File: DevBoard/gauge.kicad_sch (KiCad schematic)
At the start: 52 parts, among them J101 Pack (welded 4S) - use instea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, J102 Cell NTC 10k 103AT, J103 EV2400 SMBus, J104 Bench PACK_P, Q101 AGM404AP1, Q102 AGM404AP1, Q103 2N7002, SW101 WAKE, U101 BQ40Z50RSMR-R2

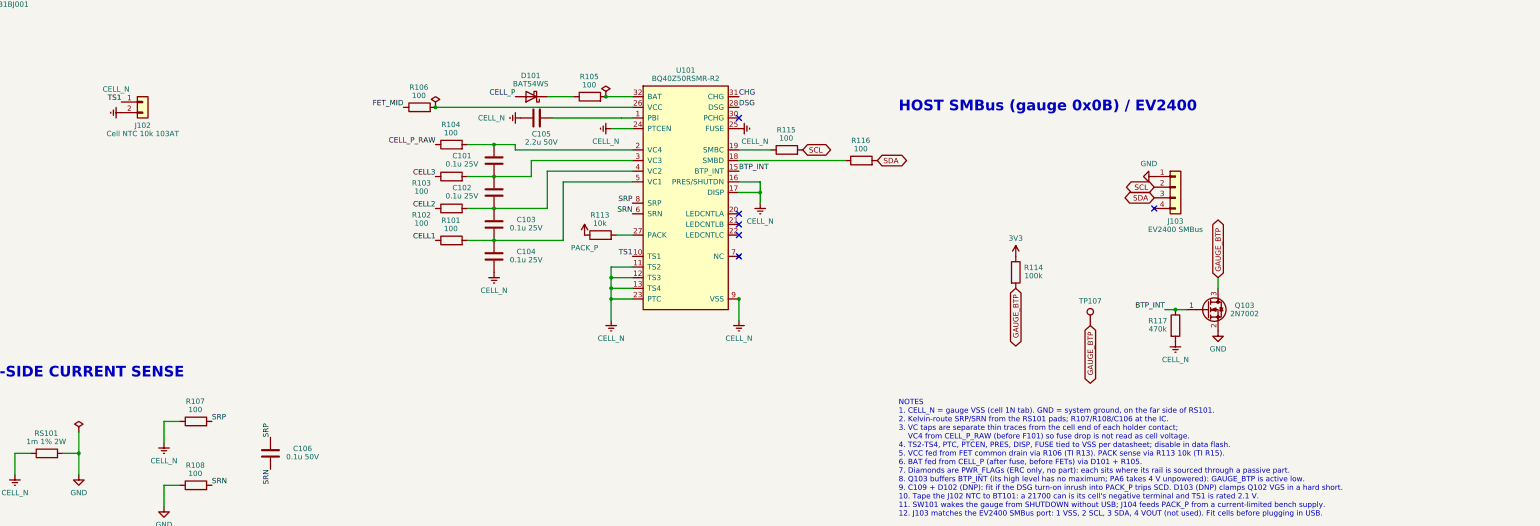
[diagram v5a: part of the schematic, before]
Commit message: Dev board: bootstrap diodes, one NTC per cell, 1 % resistors
- BQ25756 bootstrap Schottkys DRV_SUP -> BTST1/BTST2 on both ports
  (TI BQ25756 schematic checklist D2/D3, required; LRB521S-40T1G,
  SOD-523), placed in line with the BTST caps. Also added to the
  production BOM/netlist.
- Gauge TS2-TS4 no longer tied to VSS: J105-J107 take a wired 10k NTC
  per cell; all four NTC headers sit beside their cell's tap test point.
- Precision resistors rounded to stocked UNI-ROYAL 1 % parts (ICHG
  9.1k, ILIM 3.6k, TS 1.8k/5.6k, FSW/ACUV-ACOV, NTC dividers); only the
  charge-voltage and PP5V feedback dividers stay 0.1 %.

Co-Authored-By: Claude Opus 5.5 <noreply@anthropic.com>
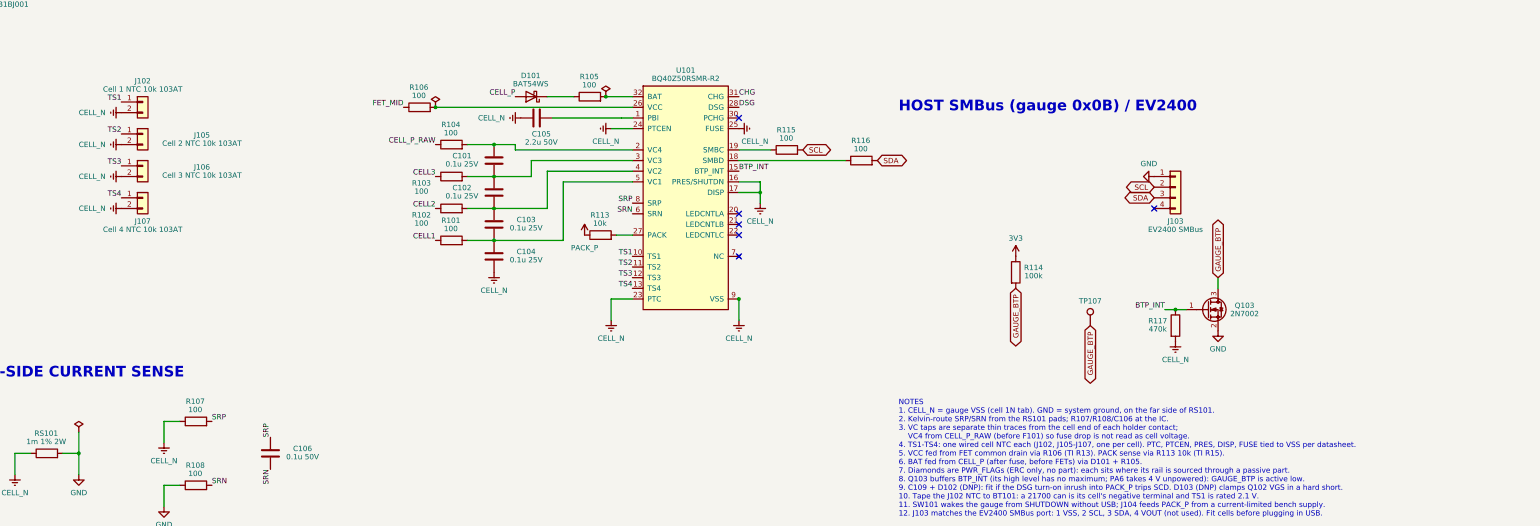
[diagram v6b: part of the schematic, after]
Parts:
- added J105: Cell 2 NTC 10k 103AT, Connector_PinHeader_2.54mm:PinHeader_1x02_P2.54mm_Vertical, symbol Connector_Generic:Conn_01x02
- added J106: Cell 3 NTC 10k 103AT, Connector_PinHeader_2.54mm:PinHeader_1x02_P2.54mm_Vertical, symbol Connector_Generic:Conn_01x02
- added J107: Cell 4 NTC 10k 103AT, Connector_PinHeader_2.54mm:PinHeader_1x02_P2.54mm_Vertical, symbol Connector_Generic:Conn_01x02
- J102: value Cell NTC 10k 103AT -> Cell 1 NTC 10k 103AT; LCSC (none) -> C492401; MPN (none) -> PZ254V-11-02P; Notes (none) -> Wired 10k B3435 NTC (Semitec 103AT-2 class, epoxy bead with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
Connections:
- net CELL_N: now also J105.2 (Pin_2), J106.2 (Pin_2), J107.2 (Pin_2); no longer U101.11 (TS2), U101.12 (TS3), U101.13 (TS4)
- new net TS2: J105.1 (Pin_1), U101.11 (TS2)
- new net TS3: J106.1 (Pin_1), U101.12 (TS3)
- new net TS4: J107.1 (Pin_1), U101.13 (TS4)
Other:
- note added: "NOTES 1. CELL_N = gauge VSS (cell 1N tab). GND = system ground, on the far side of RS101. 2. Kelvin-route SRP/SRN from the RS101 pads; R107/R108/C106 at the IC. 3. VC taps are separate thin traces from the cell end of each holder contact; VC4 from CELL_P_RAW (before F101) so fuse drop is not read as cell voltage. 4. TS1-TS4: one wired cell NTC each (J102, J105-J107, one per cell). PTC, PTCEN, PRE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"
- note removed: "NOTES 1. CELL_N = gauge VSS (cell 1N tab). GND = system ground, on the far side of RS101. 2. Kelvin-route SRP/SRN from the RS101 pads; R107/R108/C106 at the IC. 3. VC taps are separate thin traces from the cell end of each holder contact; VC4 from CELL_P_RAW (before F101) so fuse drop is not read as cell voltage. 4. TS2-TS4, PTC, PTCEN, PRES, DISP, FUSE tied to VSS per datasheet; disable in data 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"

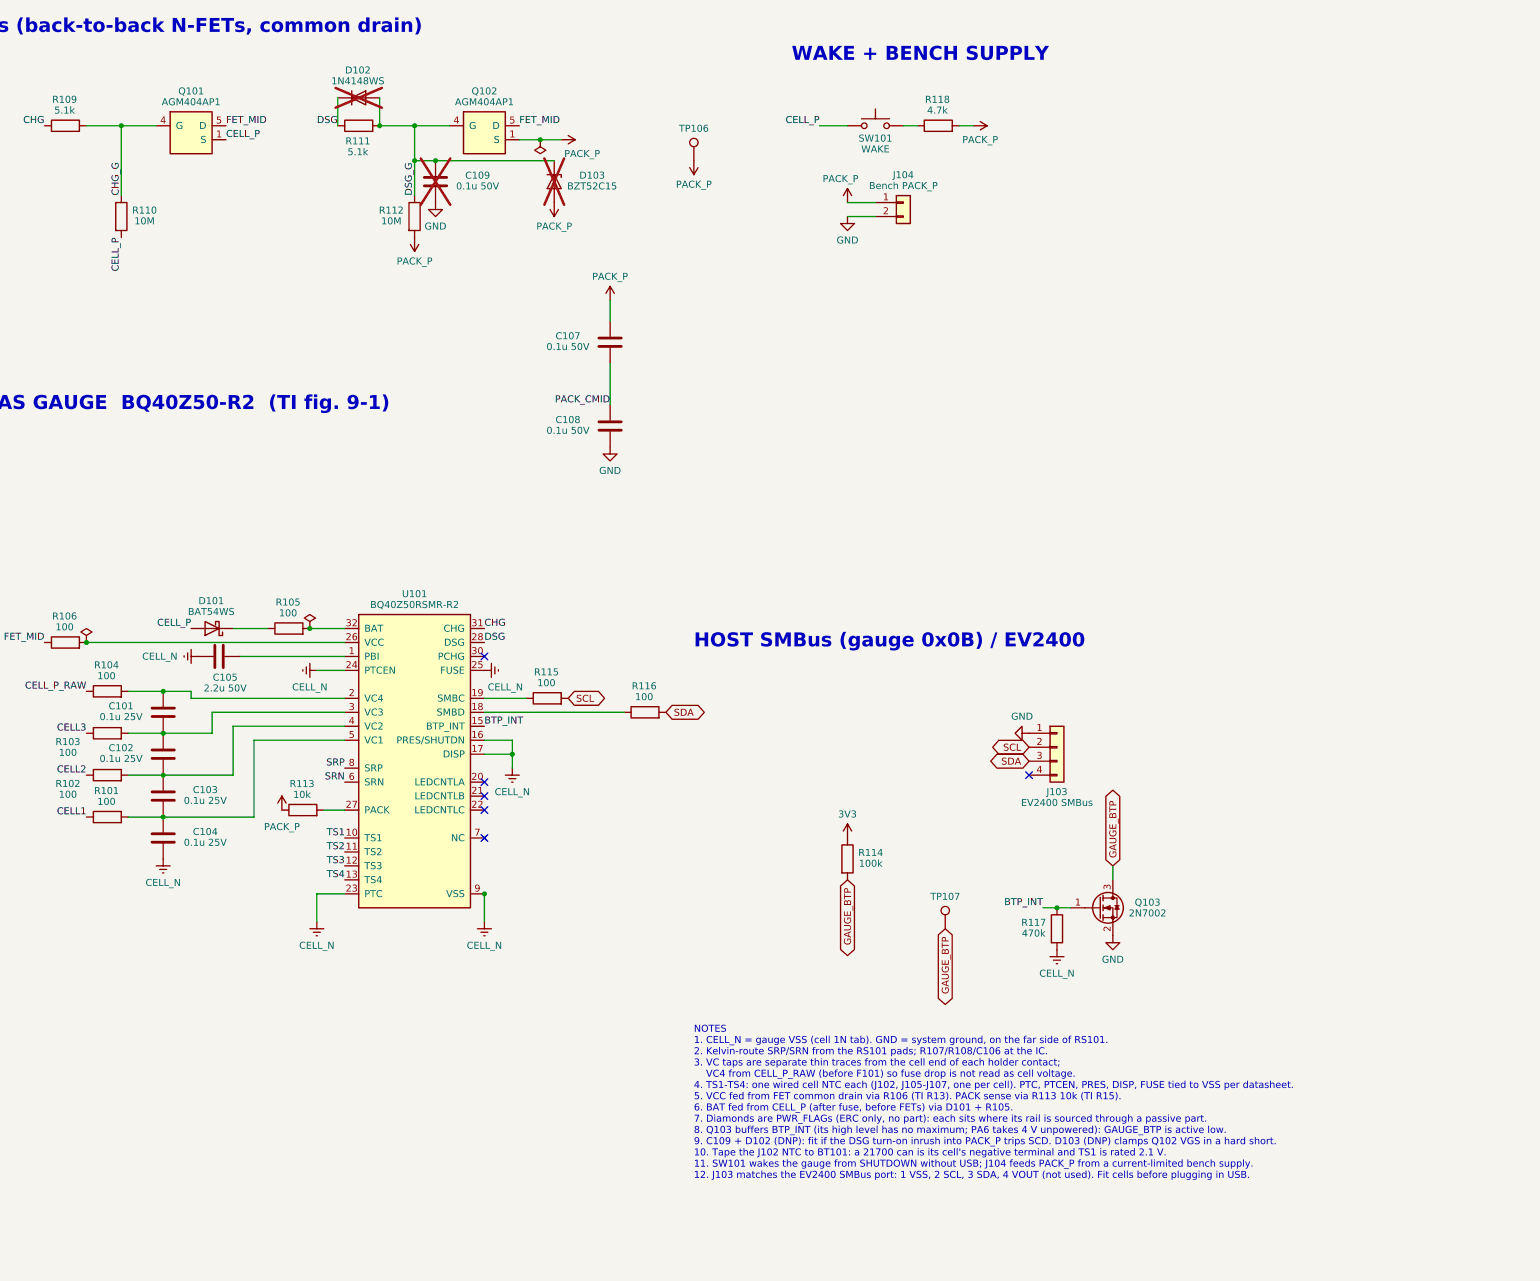
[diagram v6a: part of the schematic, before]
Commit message: Dev board rev A5: FET ESD caps, review 2, fail-safe CHG_INH, MCU I/O plan
- Gauge: C110/C111 (2 x 0.1 uF in series) across the protection FET pair,
  TI BQ40Z50-R2 fig. 9-2 C1/C2; C107/C108 across PACK+/PACK- unchanged.
- Second 3-reviewer schematic review with a challenge round
  (docs/devboard/schematic-review-2-2026-10-12.md, raw files in review2/):
  0 critical, 1 major (gauge precharge config), hardware proposals listed.
- CHG_INH now fails safe: R417/R517 47k pull-up on CE to 3V3; the MCU
  drives PB8 low to allow charging. MCU IWDG in hardware mode.
- Decisions: ICHG stays 9.1k; F101 stays 15 A with a gauge cut-off of
  2.8 V/cell or higher under load.
- docs/devboard/mcu-io-power-states.md: every MCU pin per power state,
  reconciled with the 150 uA sleep budget (PB8 low only while charging).

Co-Authored-By: Claude Opus 5.5 <noreply@anthropic.com>
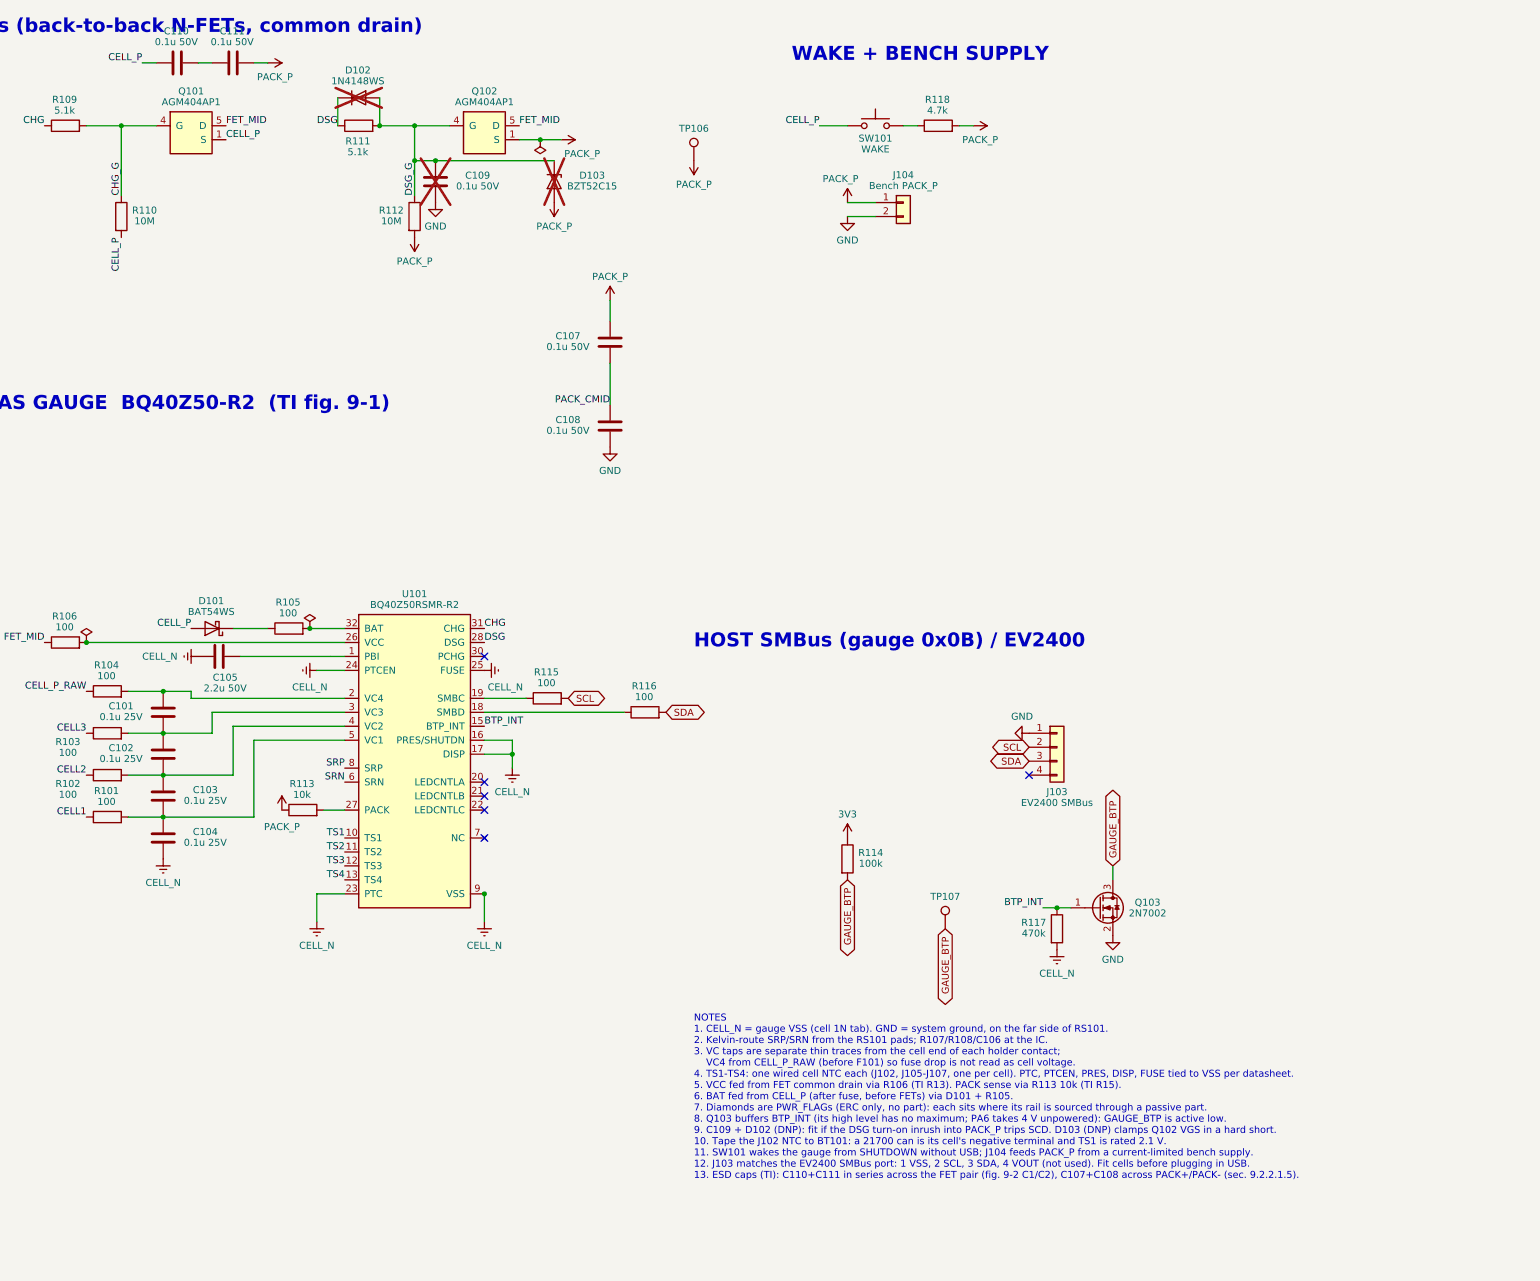
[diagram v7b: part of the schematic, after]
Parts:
- added C110, C111: 0.1u 50V, Capacitor_SMD:C_0603_1608Metric, symbol Device:C
- F101: Notes Hand-fit after checking all four cells at TP102-TP105 (JLC leaves it off). 15 A for 100 W out at the 12 V low end (~10 A continuous, 75 % derating). Interrupt 300 A at 24 Vdc (pack max 16.8 V). 3.9 mOhm: 0.4 W at 10 A, give it copper -> Hand-fit after checking all four cells at TP102-TP105 (JLC leaves it off). 15 A for 100 W out at the 12 V low end (~10 A continuous, 75 % derating). Interrupt 300 A at 24 Vdc (pack max 16.8 V). 3.9 mOhm: 0.4 W at 10 A, give it copper. Review 2 D3: 15 A holds only if the gauge cut-off under load stays at 2.8 V/cell or higher (9.8 A at 100 W); a lower cut-off needs 1206FA-20A
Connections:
- net CELL_P: now also C110.1
- net PACK_P: now also C111.2
- new net: C110.2, C111.1

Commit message: Dev board rev A5: BAT fed before F101, review 2 hardware fixes, JLC passives
- Gauge BAT feed follows TI fig. 9-12: D101 from the cell top (CELL_P_RAW)
  before F101, so the gauge stays powered if the fuse opens or is unfitted.
- C421/C521 100 uF 35 V polymer (same 6.3 mm footprint): about 99 uF worst
  case vs the BQ25756 80 uF minimum after derating.
- Bootstrap diodes LRB520S-40T1G, Q103 BSS138, DNP C109 4.7 nF (fit D103
  with it), PPHV 0.1 uF and VBUS 10 nF per port, R306 330R, C201 DNP flag.
- Test points: GND loops by each port's SW probes and in the pack probe
  field, CELL_P_RAW, CE_N, LDO_3V3, LDO_IN, 5V_AMP.
- JLC part numbers on every resistor and capacitor.
- Placement for the new parts; placer hides test-point labels with no
  free spot. DRC clean, schematic parity clean.

Co-Authored-By: Claude Opus 5.5 <noreply@anthropic.com>
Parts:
- added TP108: CELL_P_RAW, TestPoint:TestPoint_Keystone_5000-5004_Miniature, symbol Connector:TestPoint
- added TP109: GND, TestPoint:TestPoint_Keystone_5000-5004_Miniature, symbol Connector:TestPoint
- C101, C102, C103, C104: value 0.1u 25V -> 0.1u 50V; LCSC (none) -> C14663; MPN (none) -> CC0603KRX7R9BB104
- C107, C108: LCSC (none) -> C14663; MPN (none) -> CC0603KRX7R9BB104
- C109: value 0.1u 50V -> 4.7n 50V; LCSC C14663 -> C53987; MPN CC0603KRX7R9BB104 -> 0603B472K500NT; Notes DNP: fit if DSG turn-on inrush into PACK_P (~280 uF, est. 1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 -> DNP: fit only if DSG turn-on inrush trips SCD. 4.7 nF (not 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
- D101: Notes (none) -> BAT feed from the cell top before F101, as TI fig. 9-12 (D1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
- Q103: value 2N7002 -> BSS138; LCSC C8545 -> C52895; MPN 2N7002 -> BSS138 (onsemi); Notes BTP_INT level shift: its high level has no maximum, PA6 all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 -> BTP_INT level shift (inverts: GAUGE_BTP active low). BSS138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
- R105, R106, R107, R108, R115, R116: LCSC (none) -> C22775; MPN (none) -> 0603WAF1000T5E
- R109, R111: LCSC (none) -> C23186; MPN (none) -> 0603WAF5101T5E
- R110, R112: LCSC (none) -> C7250; MPN (none) -> 0603WAF1005T5E
- R113: LCSC (none) -> C25804; MPN (none) -> 0603WAF1002T5E
- R114: LCSC (none) -> C25803; MPN (none) -> 0603WAF1003T5E
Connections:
- net CELL_P: no longer D101.2 (A)
- net CELL_P_RAW: now also D101.2 (A), TP108.1
- net GND: now also TP109.1
